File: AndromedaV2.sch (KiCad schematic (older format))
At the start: 0 parts

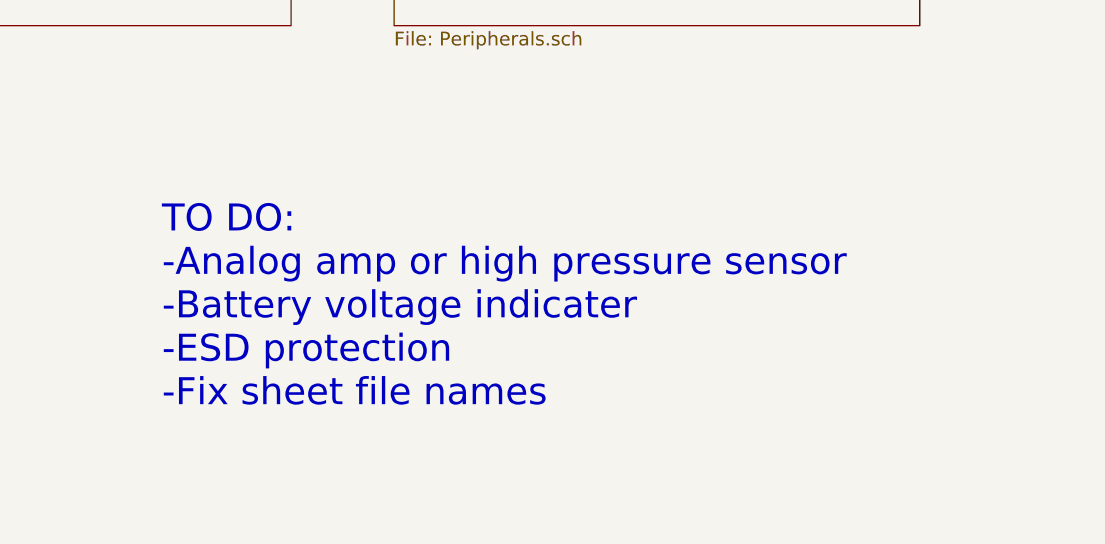
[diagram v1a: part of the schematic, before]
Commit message: Add schem documentation and generate new PDF
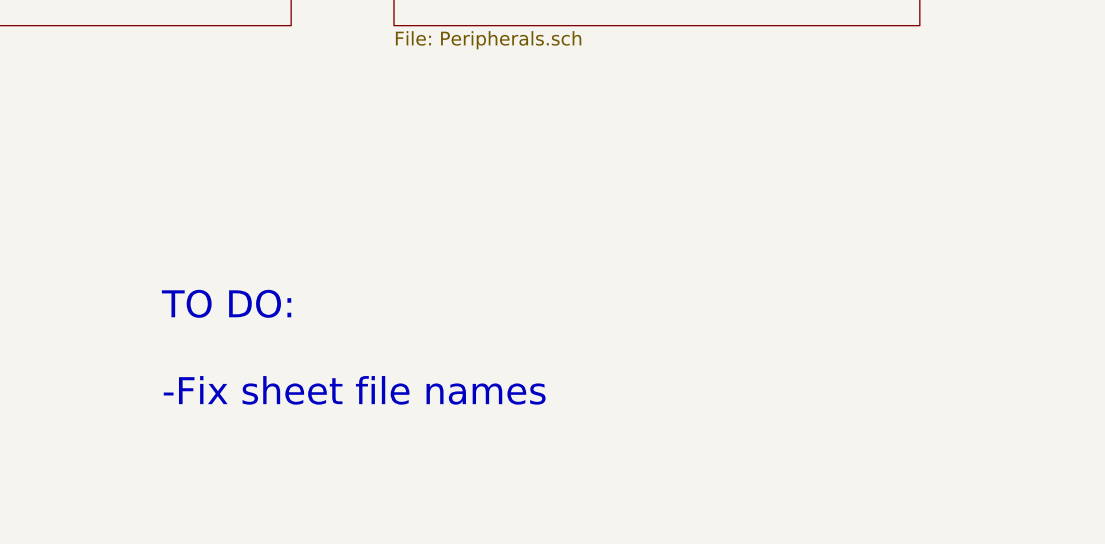
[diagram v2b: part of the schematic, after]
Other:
- note added: "TO DO:\n\n-Fix sheet file names"
- note removed: "TO DO:\n-Analog amp or high pressure sensor\n-Battery voltage indicater\n-ESD protection\n-Fix sheet file names"
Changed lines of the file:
@@
 $EndSheet
 Text Notes 6485 4980 0    118  ~ 0
-TO DO:\n-Analog amp or high pressure sensor\n-Battery voltage indicater\n-ESD protection\n-Fix sheet file names
+TO DO:\n\n-Fix sheet file names
 $EndSCHEMATC

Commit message: Changes based on review reccommemdations
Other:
- note added: "TO DO:\n\nStiching around edge for EMI\n\n\n-Fix sheet file names"
- note removed: "TO DO:\n\n-Fix sheet file names"
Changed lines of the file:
@@
 $EndSheet
 Text Notes 6485 4980 0    118  ~ 0
-TO DO:\n\n-Fix sheet file names
+TO DO:\n\nStiching around edge for EMI\n\n\n-Fix sheet file names
 $EndSCHEMATC
